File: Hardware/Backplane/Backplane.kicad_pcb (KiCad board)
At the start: 2 copper layers, 100 x 100 mm, 49 parts, among them J1 PWR_SW, J10 Conn_02x20_Odd_Even, J2 USB_C_Receptacle_USB2.0, J3 RESET_SW, J4 CLOCK_ENBL_SW, J5 Conn_02x20_Odd_Even, J6 Conn_02x20_Odd_Even, J7 Conn_02x20_Odd_Even, J8 Conn_02x20_Odd_Even, J9 Conn_02x20_Odd_Even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

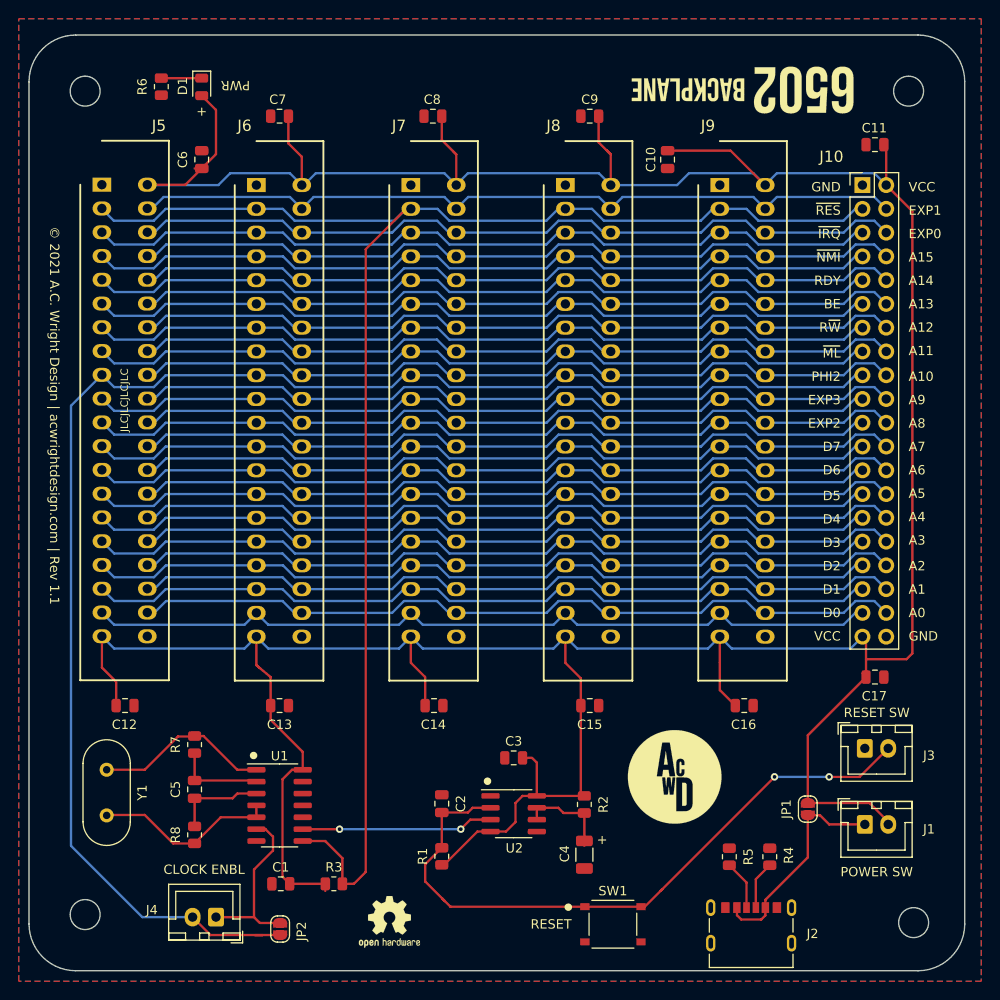
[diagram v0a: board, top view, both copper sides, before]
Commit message: Update to Kicad 8.0
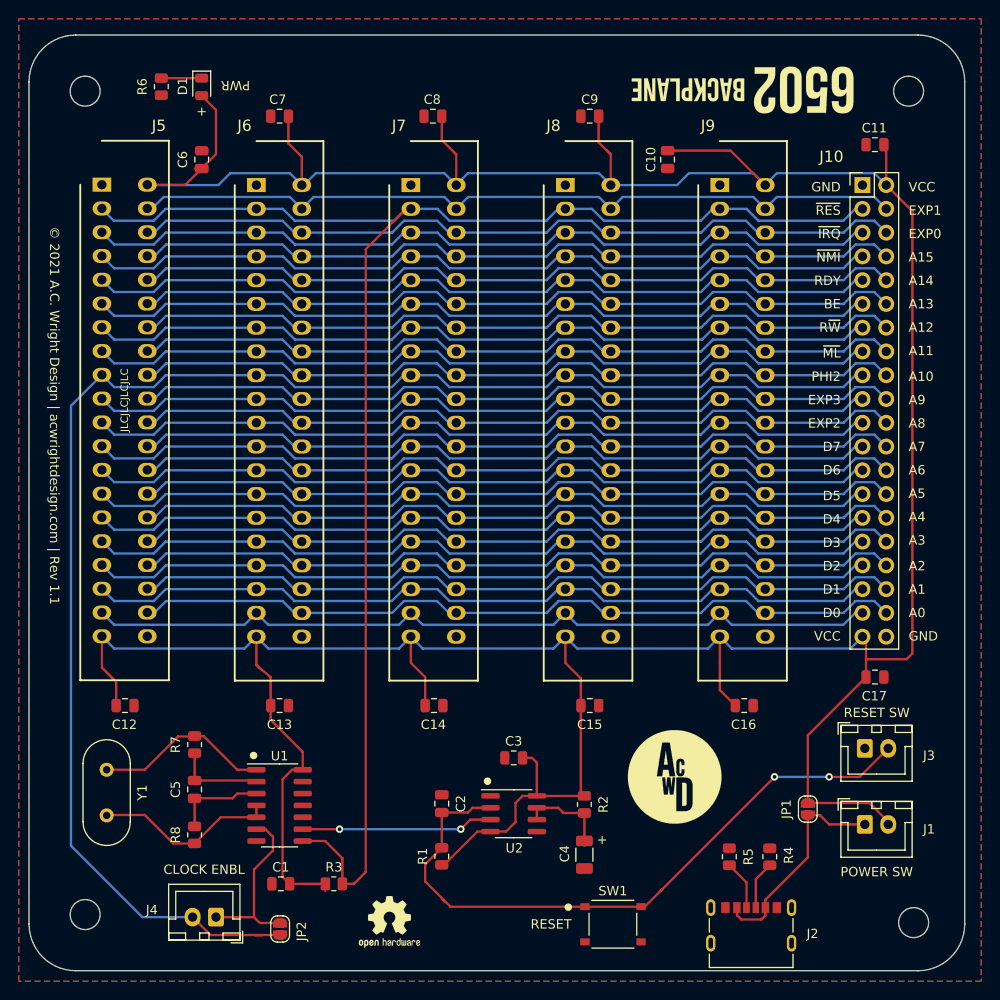
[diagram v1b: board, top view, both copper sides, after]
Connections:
- net /R~W renamed /R~{W}
- net /~IRQ renamed /~{IRQ}
- net /~ML renamed /~{ML}
- net /~NMI renamed /~{NMI}
- net ~RES renamed ~{RES}
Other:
- net class Default removed
- board text added: "R~{W}"
- board text added: "~{IRQ}"
- board text added: "~{ML}"
- board text added: "~{NMI}"
- board text added: "~{RES}"
- board text removed: "R~W"
- board text removed: "~IRQ"
- board text removed: "~ML"
- board text removed: "~NMI"
- board text removed: "~RES"

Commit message: Cleanup
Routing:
- net PHI2: track 165.4 -> 164.6 mm
- net Net-(C2-Pad1): track 71.8 -> 71.1 mm
- net VCC: track 417.7 -> 418.4 mm
- net GND: vias 0 -> 29
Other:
- board text added: "© 2024 A.C. Wright Design | acwrightdesign.com | Rev 2.0"
- board text removed: "© 2021 A.C. Wright Design | acwrightdesign.com | Rev 1.1"

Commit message: Cleanup
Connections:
- net /R~{W} renamed /RWB
- net /~{IRQ} renamed /IRQB
- net /~{ML} renamed /MLB
- net /~{NMI} renamed /NMIB
- net ~{RES} renamed RESB
- U1 pad 10: Net-(U1-Pad10) -> unconnected-(U1-Pad10)
- U1 pad 12: Net-(U1-Pad12) -> unconnected-(U1-Pad12)
- U2 pad 5: Net-(U2-Pad5) -> unconnected-(U2-CV-Pad5)
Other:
- board text added: "IRQB"
- board text added: "MLB"
- board text added: "NMIB"
- board text added: "RESB"
- board text added: "RWB"
- board text removed: "R~{W}"
- board text removed: "~{IRQ}"
- board text removed: "~{ML}"
- board text removed: "~{NMI}"
- board text removed: "~{RES}"

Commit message: Updates
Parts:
- added D2: 1N5819, Diode_SMD:D_SOD-323F, F.Cu at (173.2, 125.8)
- added TP1: 5V, TestPoint:TestPoint_Pad_1.0x1.0mm, F.Cu at (173.2, 120.0)
- added TP2: CLK, TestPoint:TestPoint_Pad_1.0x1.0mm, F.Cu at (122.6, 144.8)
- added TP3: RESET, TestPoint:TestPoint_Pad_1.0x1.0mm, F.Cu at (122.4, 124.0)
- added TP4: GND, TestPoint:TestPoint_Pad_1.0x1.0mm, F.Cu at (129.0, 127.2)
- J2: footprint Backplane:CUI_UJC-HP-3-SMT-TR -> Connector_USB:USB_C_Receptacle_HRO_TYPE-C-31-M-12
- SW1: value SW_Push -> Reset
- moved J2 2.59 mm to (167.2, 145.8)
- moved R4 0.26 mm to (168.9, 137.8)
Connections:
- J1 pad 2: VCC -> Net-(D2-A)
- JP1 pad 2: VCC -> Net-(D2-A)
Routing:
- net Net-(D2-A): track 0.00 -> 14.9 mm
- net VCC: track 418.4 -> 404.2 mm
- net Net-(J4-Pin_1): track 18.7 -> 24.5 mm
- net RESB: track 170.5 -> 174.1 mm
- net Net-(J2-CC2): track 5.14 -> 3.08 mm
- net Net-(J2-CC1): track 5.28 -> 3.52 mm
- net GND: track 0.00 -> 1.45 mm

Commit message: Working on new PCBs
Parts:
- G***: footprint 6502 Logo:6502 Logo 5mm -> 6502 Logos:6502 Backplane Logo 5mm
- J5, J6, J7, J8, J9: footprint Backplane:RHDR40W82P485X254_2X20_5740X93 -> 6502 Parts:RHDR40W82P485X254_2X20_5740X93
- SW1: footprint Backplane:SW_TS-1187A-B-A-B -> 6502 Parts:SW_TS-1187A-B-A-B
- moved R4 9.69 mm to (175.4, 145.0), turned to 180 degrees
- moved R5 9.21 mm to (159.1, 145.0), turned to 0 degrees
- moved J10 0.08 mm to (179.0, 66.0)
- moved J9 0.05 mm to (163.8, 66.0)
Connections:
- net /MLB renamed /SYNC
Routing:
- net Net-(J2-CC2): track 3.08 -> 8.33 mm
- net VCC: track 404.2 -> 409.4 mm
- net Net-(J2-CC1): track 3.52 -> 8.44 mm
- net Net-(J3-Pin_2): track 71.1 -> 72.0 mm, vias 2 -> 1
- net GND: vias 29 -> 34
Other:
- board text added: "SYNC"
- board text added: "© 2024 A.C. Wright Design | acwrightdesign.com | Rev 1.0"
- board text removed: "MLB"
- board text removed: "© 2024 A.C. Wright Design | acwrightdesign.com | Rev 2.0"

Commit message: Pi Card PCB
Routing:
- net GND: track 1.45 -> 0.16 mm
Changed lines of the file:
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@@
 		(sheetname "Root")
 		(sheetfile "Backplane.kicad_sch")
+		(zone_connect 2)
 		(attr smd)
 		(fp_line
@@
 			(pintype "passive")
 		)
-		(model "${KICAD8_3DMODEL_DIR}/Connector_USB.3dshapes/USB_C_Receptacle_HRO_TYPE-C-31-M-12.wrl"
+		(model "${KIPRJMOD}/../../CAD/HRO_TYPE-C-31-M-12.step"
 			(offset
-				(xyz 0 0 0)
+				(xyz -4.52 -3.66 0.1)
 			)
 			(scale
@@
 		(layer "F.Cu")
 		(at 114.3 66 -90)
-		(descr "<b>5-5530843-4</b><br>\r")
+		(descr "<b>5-5530843-4</b><br>\n")
 		(property "Reference" "J6"
 			(at -6.35 1.27 180)
@@
 			)
 		)
-		(property ki_fp_filters "Connector*:*_2x??_*")
-		(sheetname "Root")
-		(sheetfile "Backplane.kicad_sch")
 		(attr through_hole)
 		(fp_line
-			(start 0 2.312)
-			(end 52.959 2.312)
+			(start 52.959 2.312)
+			(end 52.959 -7.162)
 			(stroke
 				(width 0.2)
@@
 		)
 		(fp_line
-			(start 52.959 2.312)
-			(end 52.959 -7.162)
+			(start -4.7 2.3)
+			(end 52.959 2.312)
 			(stroke
 				(width 0.2)
@@
 		(fp_line
 			(start -4.699 -7.162)
-			(end -4.699 0)
+			(end -4.7 2.3)
 			(stroke
 				(width 0.2)
@@
 			(solder_mask_margin 0.1016)
 		)
-		(model "/Users/acwright/Library/Mobile Documents/com~apple~CloudDocs/Documents/Projects/6502 8-Bit Computer/6502/CAD/5-5530843-4.step"
+		(model "${KIPRJMOD}/../../CAD/5-5530843-4.step"
 			(offset
 				(xyz 24.5 2.5 15.5)
@@
 		(layer "F.Cu")
 		(at 130.8 66 -90)
-		(descr "<b>5-5530843-4</b><br>\r")
+		(descr "<b>5-5530843-4</b><br>\n")
 		(property "Reference" "J7"
 			(at -6.35 1.27 180)
@@
 			)
 		)
-		(property ki_fp_filters "Connector*:*_2x??_*")
-		(sheetname "Root")
-		(sheetfile "Backplane.kicad_sch")
 		(attr through_hole)
 		(fp_line
-			(start 0 2.312)
-			(end 52.959 2.312)
+			(start 52.959 2.312)
+			(end 52.959 -7.162)
 			(stroke
 				(width 0.2)
@@
 		)
 		(fp_line
-			(start 52.959 2.312)
-			(end 52.959 -7.162)
+			(start -4.7 2.3)
+			(end 52.959 2.312)
 			(stroke
 				(width 0.2)
@@
 		(fp_line
 			(start -4.699 -7.162)
-			(end -4.699 0)
+			(end -4.7 2.3)
 			(stroke
 				(width 0.2)
@@
 			(solder_mask_margin 0.1016)
 		)
-		(model "/Users/acwright/Library/Mobile Documents/com~apple~CloudDocs/Documents/Projects/6502 8-Bit Computer/6502/CAD/5-5530843-4.step"
+		(model "${KIPRJMOD}/../../CAD/5-5530843-4.step"
 			(offset
 				(xyz 24.5 2.5 15.5)
@@
 		(layer "F.Cu")
 		(at 147.3 66 -90)
-		(descr "<b>5-5530843-4</b><br>\r")
+		(descr "<b>5-5530843-4</b><br>\n")
 		(property "Reference" "J8"
 			(at -6.35 1.27 180)
@@
 			)
 		)
-		(property ki_fp_filters "Connector*:*_2x??_*")
-		(sheetname "Root")
-		(sheetfile "Backplane.kicad_sch")
 		(attr through_hole)
 		(fp_line
-			(start 0 2.312)
-			(end 52.959 2.312)
+			(start 52.959 2.312)
+			(end 52.959 -7.162)
 			(stroke
 				(width 0.2)
@@
 		)
 		(fp_line
-			(start 52.959 2.312)
-			(end 52.959 -7.162)
+			(start -4.7 2.3)
+			(end 52.959 2.312)
 			(stroke
 				(width 0.2)
@@
 		(fp_line
 			(start -4.699 -7.162)
-			(end -4.699 0)
+			(end -4.7 2.3)
 			(stroke
 				(width 0.2)
@@
 			(solder_mask_margin 0.1016)
 		)
-		(model "/Users/acwright/Library/Mobile Documents/com~apple~CloudDocs/Documents/Projects/6502 8-Bit Computer/6502/CAD/5-5530843-4.step"
+		(model "${KIPRJMOD}/../../CAD/5-5530843-4.step"
 			(offset
 				(xyz 24.5 2.5 15.5)
@@
 		(layer "F.Cu")
 		(at 163.8 66 -90)
-		(descr "<b>5-5530843-4</b><br>\r")
+		(descr "<b>5-5530843-4</b><br>\n")
 		(property "Reference" "J9"
 			(at -6.35 1.27 180)
@@
 			)
 		)
-		(property ki_fp_filters "Connector*:*_2x??_*")
-		(sheetname "Root")
-		(sheetfile "Backplane.kicad_sch")
 		(attr through_hole)
 		(fp_line
-			(start 0 2.312)
-			(end 52.959 2.312)
+			(start 52.959 2.312)
+			(end 52.959 -7.162)
 			(stroke
 				(width 0.2)
@@
 		)
 		(fp_line
-			(start 52.959 2.312)
-			(end 52.959 -7.162)
+			(start -4.7 2.3)
+			(end 52.959 2.312)
 			(stroke
 				(width 0.2)
@@
 		(fp_line
 			(start -4.699 -7.162)
-			(end -4.699 0)
+			(end -4.7 2.3)
 			(stroke
 				(width 0.2)
@@
 			(solder_mask_margin 0.1016)
 		)
-		(model "/Users/acwright/Library/Mobile Documents/com~apple~CloudDocs/Documents/Projects/6502 8-Bit Computer/6502/CAD/5-5530843-4.step"
+		(model "${KIPRJMOD}/../../CAD/5-5530843-4.step"
 			(offset
 				(xyz 24.5 2.5 15.5)
@@
 		(layer "F.Cu")
 		(at 97.8 66 -90)
-		(descr "<b>5-5530843-4</b><br>\r")
+		(descr "<b>5-5530843-4</b><br>\n")
 		(property "Reference" "J5"
 			(at -6.35 1.27 180)
@@
 			)
 		)
-		(property ki_fp_filters "Connector*:*_2x??_*")
-		(sheetname "Root")
-		(sheetfile "Backplane.kicad_sch")
 		(attr through_hole)
 		(fp_line
-			(start 0 2.312)
-			(end 52.959 2.312)
+			(start 52.959 2.312)
+			(end 52.959 -7.162)
 			(stroke
 				(width 0.2)
@@
 		)
 		(fp_line
-			(start 52.959 2.312)
-			(end 52.959 -7.162)
+			(start -4.7 2.3)
+			(end 52.959 2.312)
 			(stroke
 				(width 0.2)
@@
 		(fp_line
 			(start -4.699 -7.162)
-			(end -4.699 0)
+			(end -4.7 2.3)
 			(stroke
 				(width 0.2)
@@
 			(solder_mask_margin 0.1016)
 		)
-		(model "/Users/acwright/Library/Mobile Documents/com~apple~CloudDocs/Documents/Projects/6502 8-Bit Computer/6502/CAD/5-5530843-4.step"
+		(model "${KIPRJMOD}/../../CAD/5-5530843-4.step"
 			(offset
 				(xyz 24.5 2.5 15.5)
@@
 			)
 		)
-		(sheetname "Root")
-		(sheetfile "Backplane.kicad_sch")
 		(attr through_hole)
 		(fp_line
@@
 			(pintype "passive")
 		)
-		(model "/Users/acwright/Library/Mobile Documents/com~apple~CloudDocs/Documents/Projects/6502 8-Bit Computer/6502/CAD/TS-1187A-B-A-B.step"
+		(model "${KIPRJMOD}/../../CAD/TS-1187A-B-A-B.step"
 			(offset
 				(xyz 0 0 0)
@@
 	)
 	(segment
-		(start 170.581 141.8)
-		(end 171.496 142.715)
-		(width 0.25)
-		(layer "F.Cu")
-		(net 1)
-	)
-	(segment
 		(start 170.426 141.8)
 		(end 170.581 141.8)
@@
 	)
 	(segment
-		(start 173.228 133.38)
-		(end 174.528 133.38)
+		(start 164.726 140.825)
+		(end 165.851 139.7)
 		(width 0.5)
 		(layer "F.Cu")
@@
 	)
 	(segment
-		(start 164.726 140.825)
-		(end 165.551 140)
+		(start 173.228 133.38)
+		(end 174.528 133.38)
 		(width 0.5)
 		(layer "F.Cu")
@@
 	)
 	(segment
-		(start 169.626 139.124)
-		(end 170.25 138.5)
+		(start 164.726 141.8)
+		(end 164.726 140.825)
 		(width 0.5)
 		(layer "F.Cu")
@@
 	)
 	(segment
-		(start 164.726 141.8)
-		(end 164.726 140.825)
+		(start 169.626 139.124)
+		(end 170.25 138.5)
 		(width 0.5)
 		(layer "F.Cu")
@@
 	)
 	(segment
-		(start 165.551 140)
-		(end 169.626 140)
+		(start 170.25 138.5)
+		(end 172.5 138.5)
 		(width 0.5)
 		(layer "F.Cu")
@@
 	)
 	(segment
-		(start 170.25 138.5)
-		(end 172.5 138.5)
+		(start 165.851 139.7)
+		(end 169.626 139.7)
 		(width 0.5)
 		(layer "F.Cu")
@@
 	)
 	(segment
-		(start 168.9 141.774)
-		(end 168.926 141.8)
-		(width 0.25)
-		(layer "F.Cu")
-		(net 37)
-	)
-	(segment
 		(start 165.926 143.824)
 		(end 165.926 141.8)
@@
 		(layer "F.Cu")
 		(hatch edge 0.508)
-		(connect_pads yes
+		(connect_pads
 			(clearance 0.254)
 		)
@@
 		(filled_areas_thickness no)
 		(fill yes
-			(thermal_gap 0.508)
-			(thermal_bridge_width 0.508)
+			(thermal_gap 0.254)
+			(thermal_bridge_width 0.254)
 		)
 		(polygon
@@
 		(filled_areas_thickness no)
 		(fill yes
-			(thermal_gap 0.508)
-			(thermal_bridge_width 0.508)
+			(thermal_gap 0.254)
+			(thermal_bridge_width 0.254)
 		)
 		(polygon

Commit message: Dev Board PCB
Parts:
- moved H3 1.02 mm to (184.0, 144.0)
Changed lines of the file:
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@@
 	(footprint "MountingHole:MountingHole_3.2mm_M3"
 		(layer "F.Cu")
-		(at 184.54 144.86)
+		(at 184 144)
 		(descr "Mounting Hole 3.2mm, no annular, M3")
 		(tags "mounting hole 3.2mm no annular m3")
